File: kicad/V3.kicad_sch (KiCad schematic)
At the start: 6 parts, among them SW1 Slide_Switch_SPDT_P3mm_10x5x1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

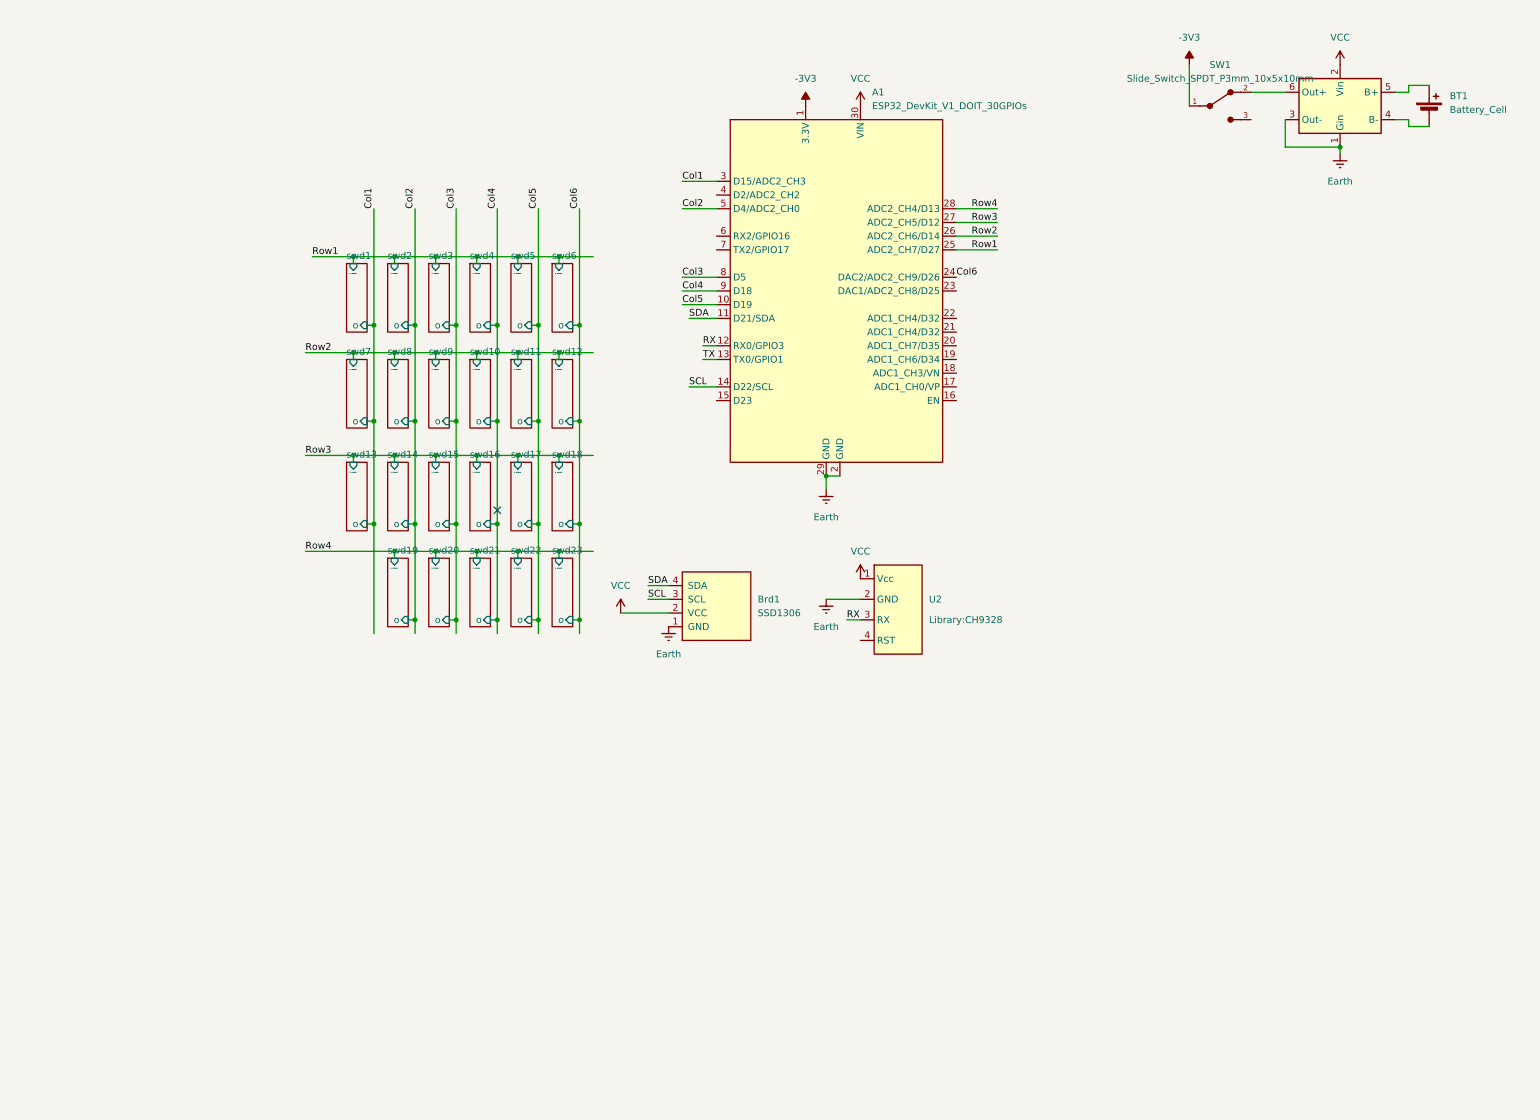
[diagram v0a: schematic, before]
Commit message: power
shouldnt be charging and discharging now i think
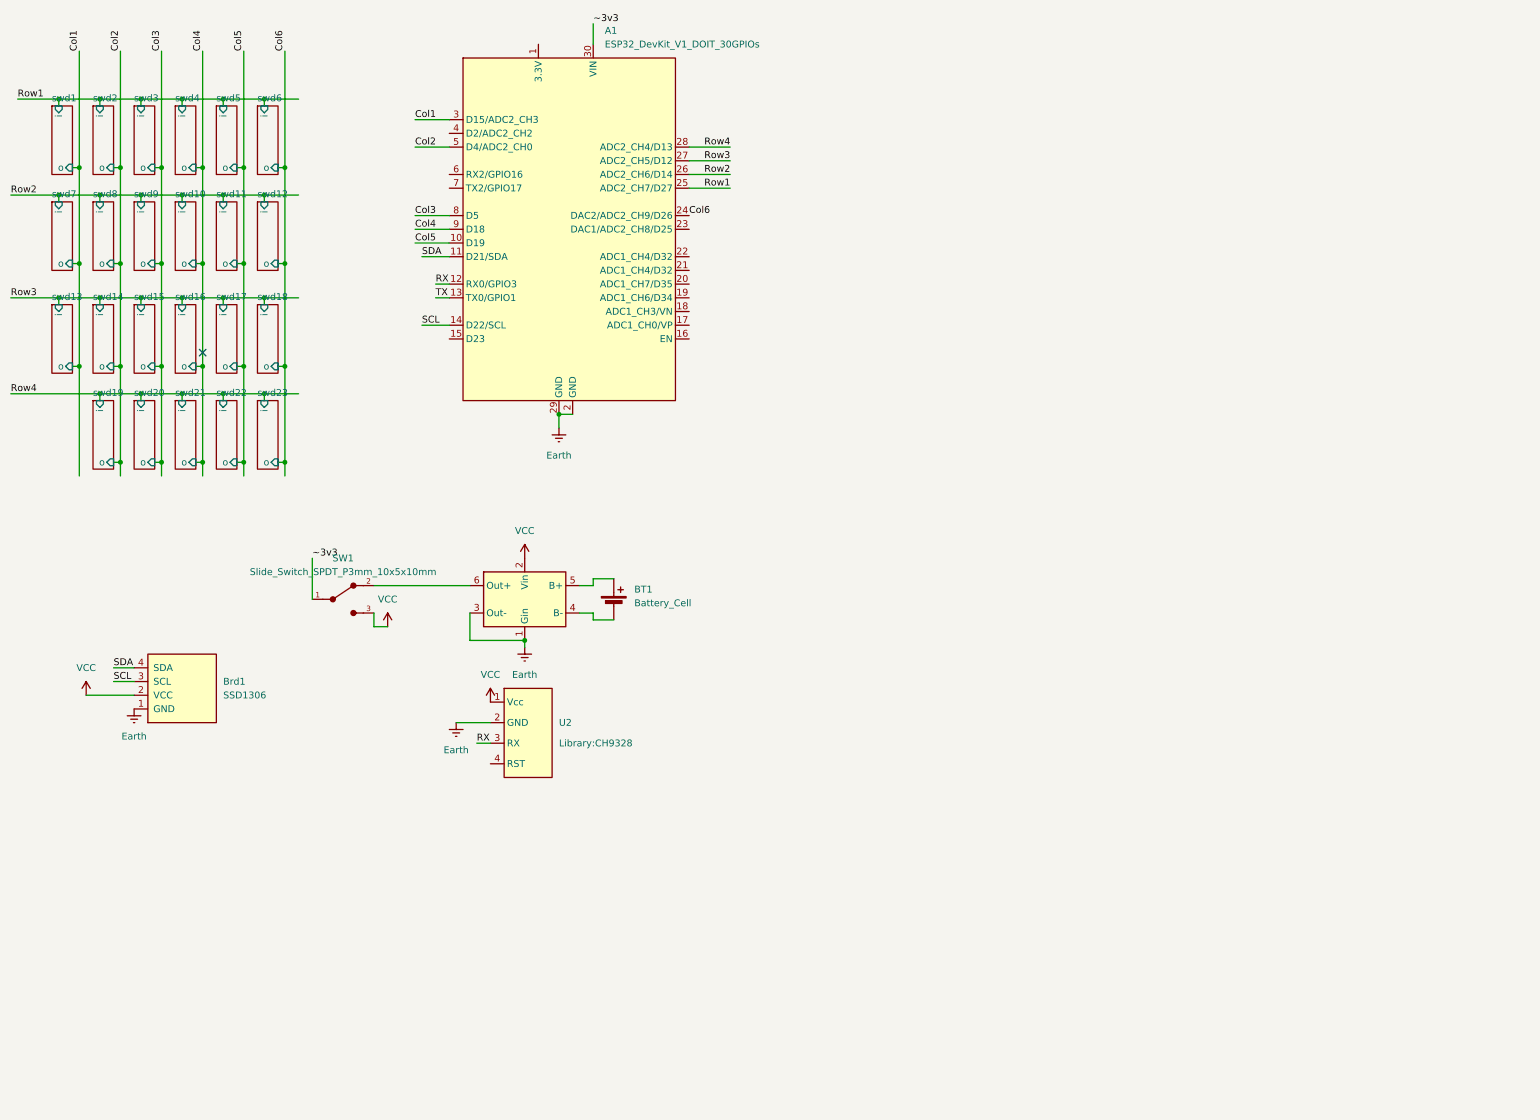
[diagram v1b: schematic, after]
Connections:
- net VCC: now also SW1.3; no longer A1.30 (VIN)
- net -3V3: no longer names the net of A1.1 (3.3V)
- net -3V3: no longer SW1.1
- new net ~3v3: A1.30 (VIN), SW1.1
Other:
- moved on the sheet: A1, BT1, Brd1, SW1, U2

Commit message: lots of changes
usb module support and more fixed wirign
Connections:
- net ~3v3: now also Brd1.2 (VCC)
- net USB_rst: now reaches A1.20 (ADC1_CH7/D35)
- net USB_rst: now also U2.4 (RST)
- net VCC renamed +5V
- net +5V: no longer Brd1.2 (VCC)
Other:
- moved on the sheet: SW1

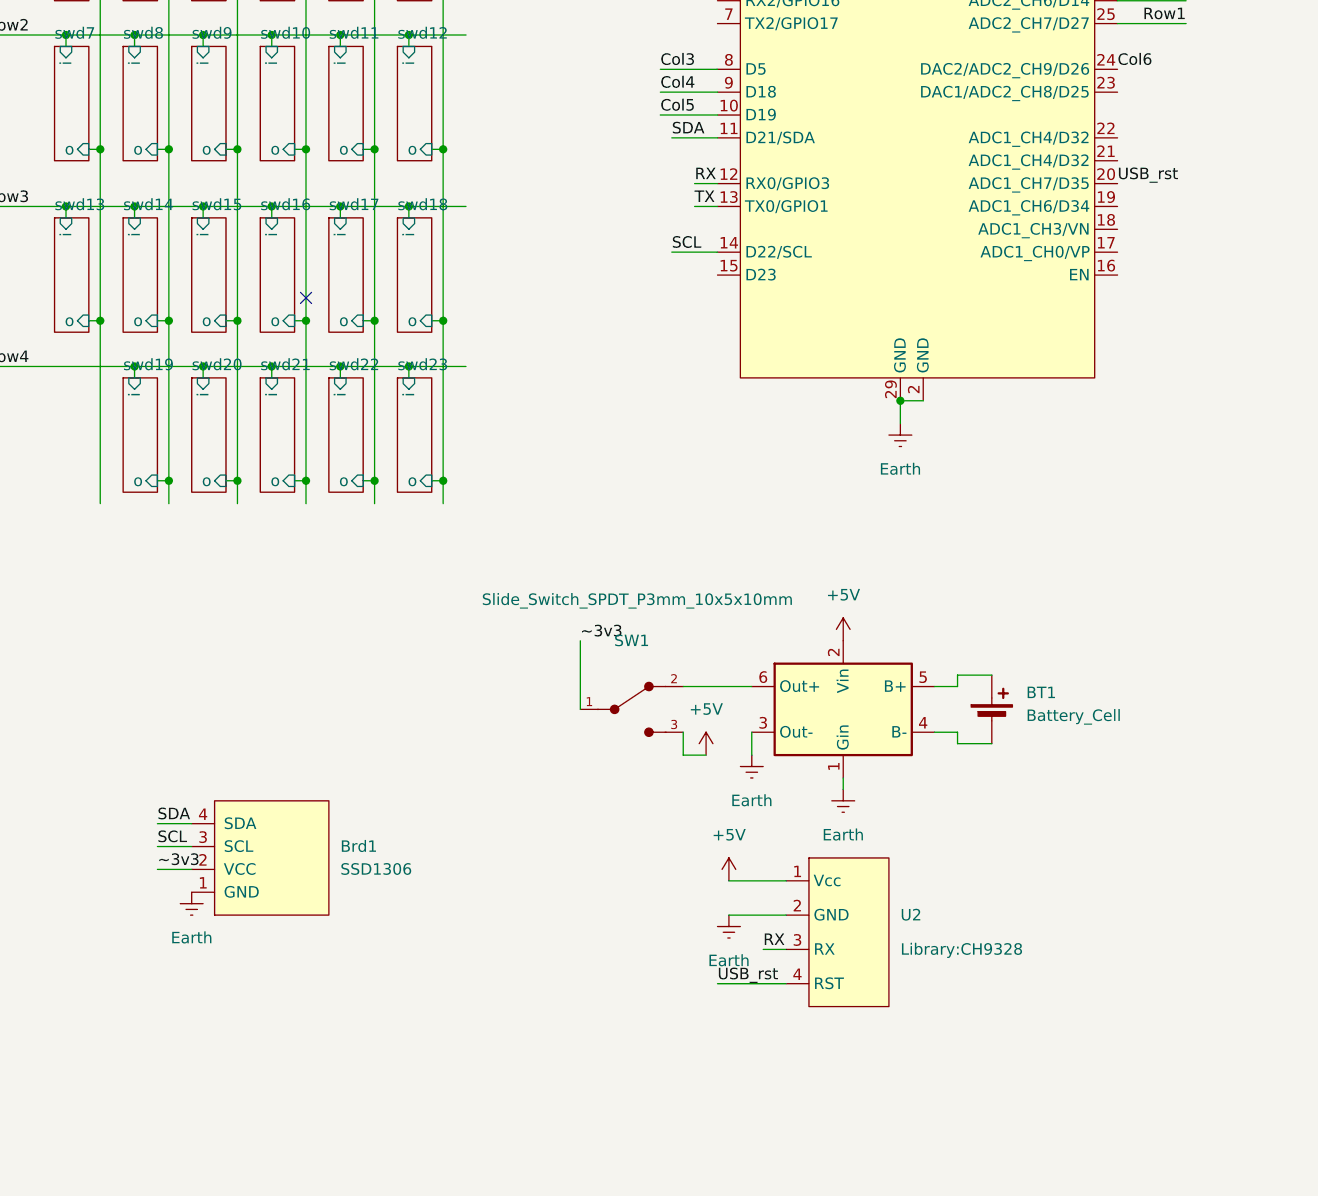
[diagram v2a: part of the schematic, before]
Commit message: schmatic changes
voltage divider now used for batter ypercentage calculation.
power-OR used as voltage supply
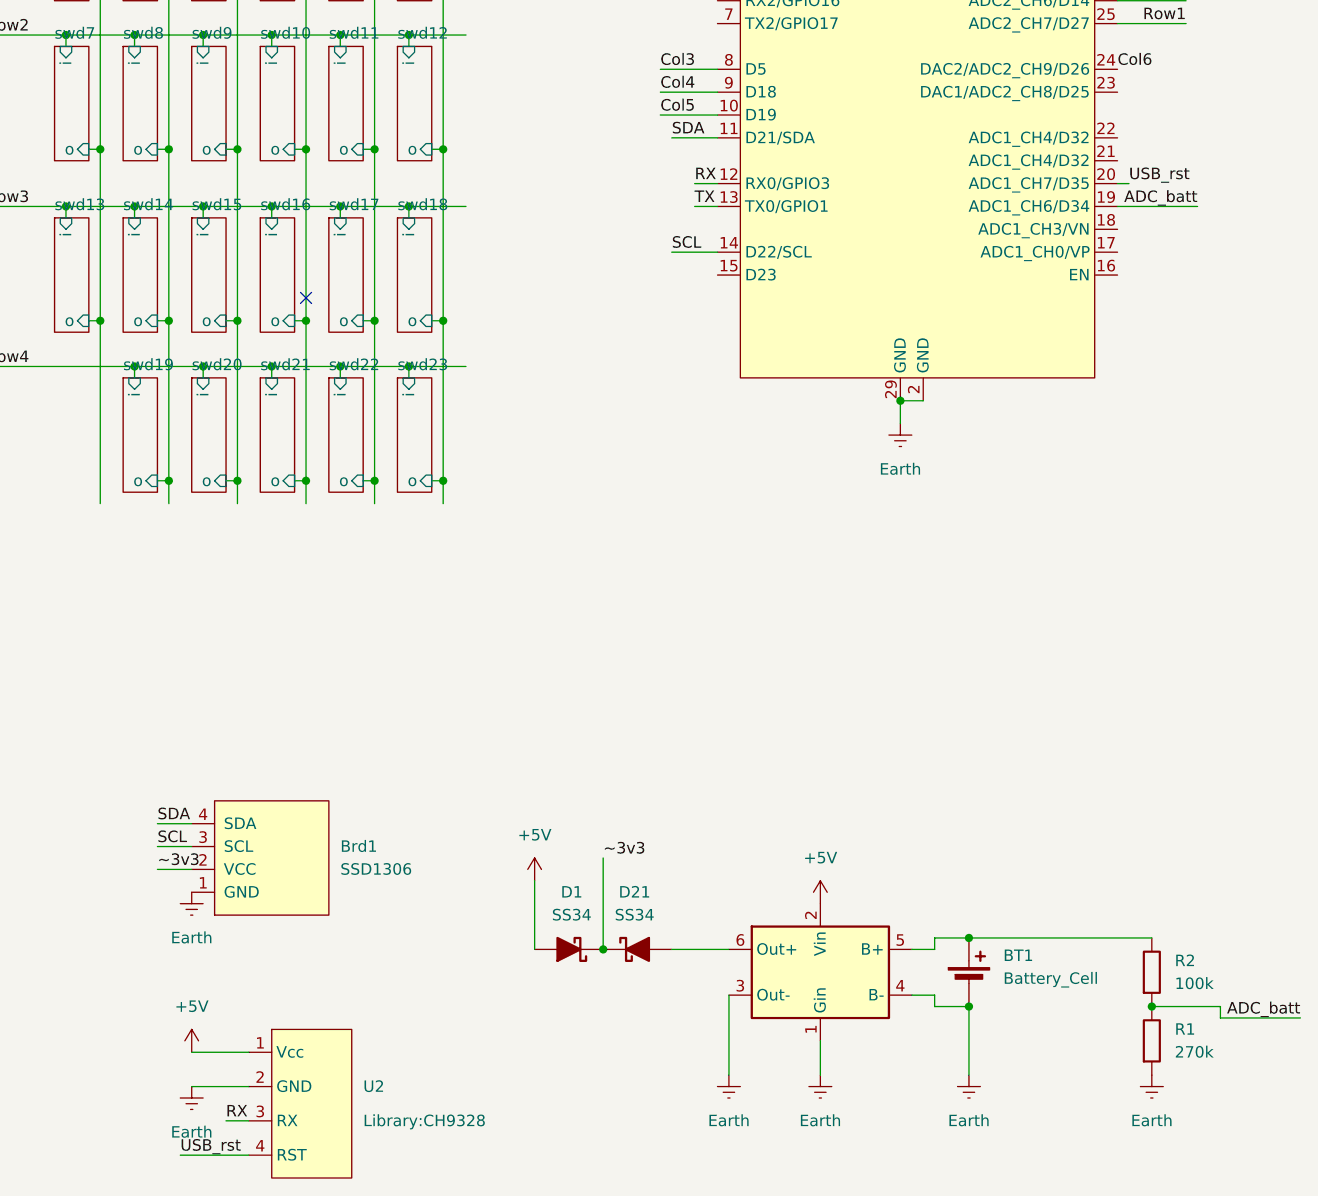
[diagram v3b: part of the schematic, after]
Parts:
- removed SW1: Slide_Switch_SPDT_P3mm_10x5x10mm, PCM_SL_Devices:Slide_Switch_SPDT_P3mm_10x5x10mm, symbol PCM_SL_Devices:Slide_Switch_SPDT_P3mm_10x5x10mm
- added D1, D21: SS34, PCM_Diode_SMD_AKL:D_SMC, symbol PCM_Diode_Schottky_AKL:SS34
- added R1: 270k, Resistor_THT:R_Axial_DIN0207_L6.3mm_D2.5mm_P10.16mm_Horizontal, symbol PCM_SL_Resistors:270k
- added R2: 100k, Resistor_THT:R_Axial_DIN0207_L6.3mm_D2.5mm_P10.16mm_Horizontal, symbol PCM_SL_Resistors:100k
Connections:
- net +5V: now also D1.2 (A)
- net Earth: now also BT1.2 (-), U1.4 (B-), R1.1
- net ~3v3: now also D1.1 (K), D21.1 (K)
- net ADC_batt: now reaches A1.19 (ADC1_CH6/D34)
- net ADC_batt: now also R1.2, R2.1
- net at BT1.1 (+), U1.5 (B+): now also R2.2
- net at U1.6 (Out+): now also D21.2 (A)
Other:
- moved on the sheet: BT1, U2

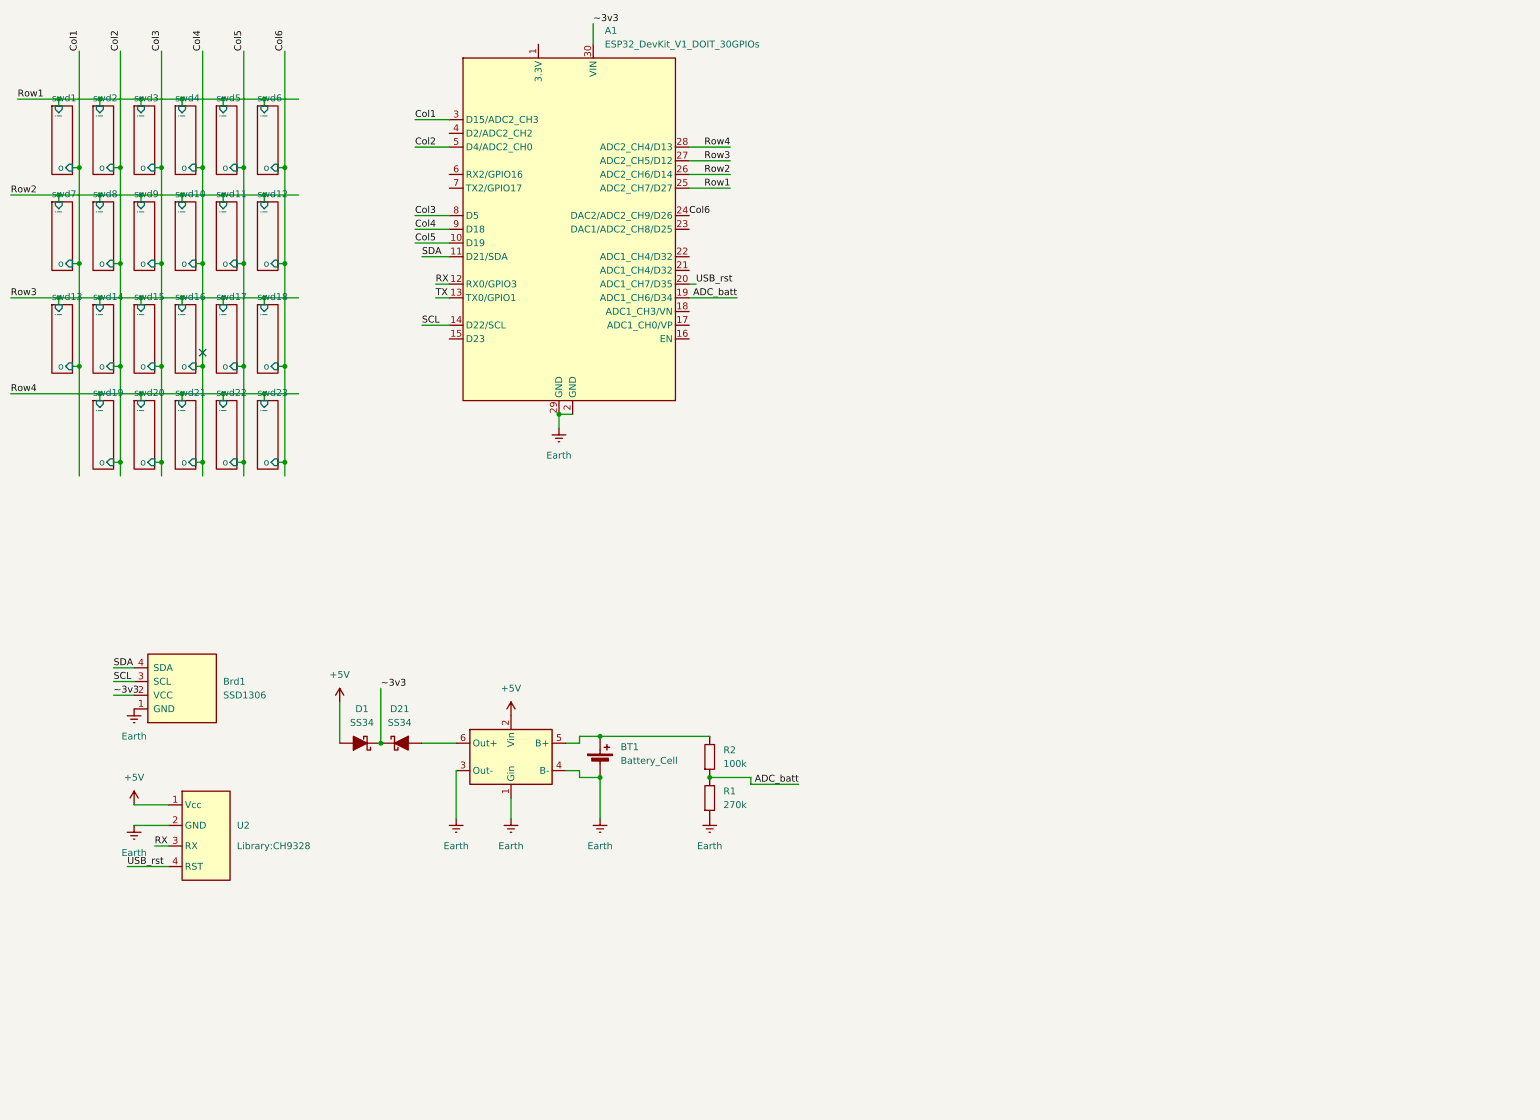
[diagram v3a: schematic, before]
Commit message: chip change
changed the module to use the ch9329(chip) instead of the ch9328 (board)
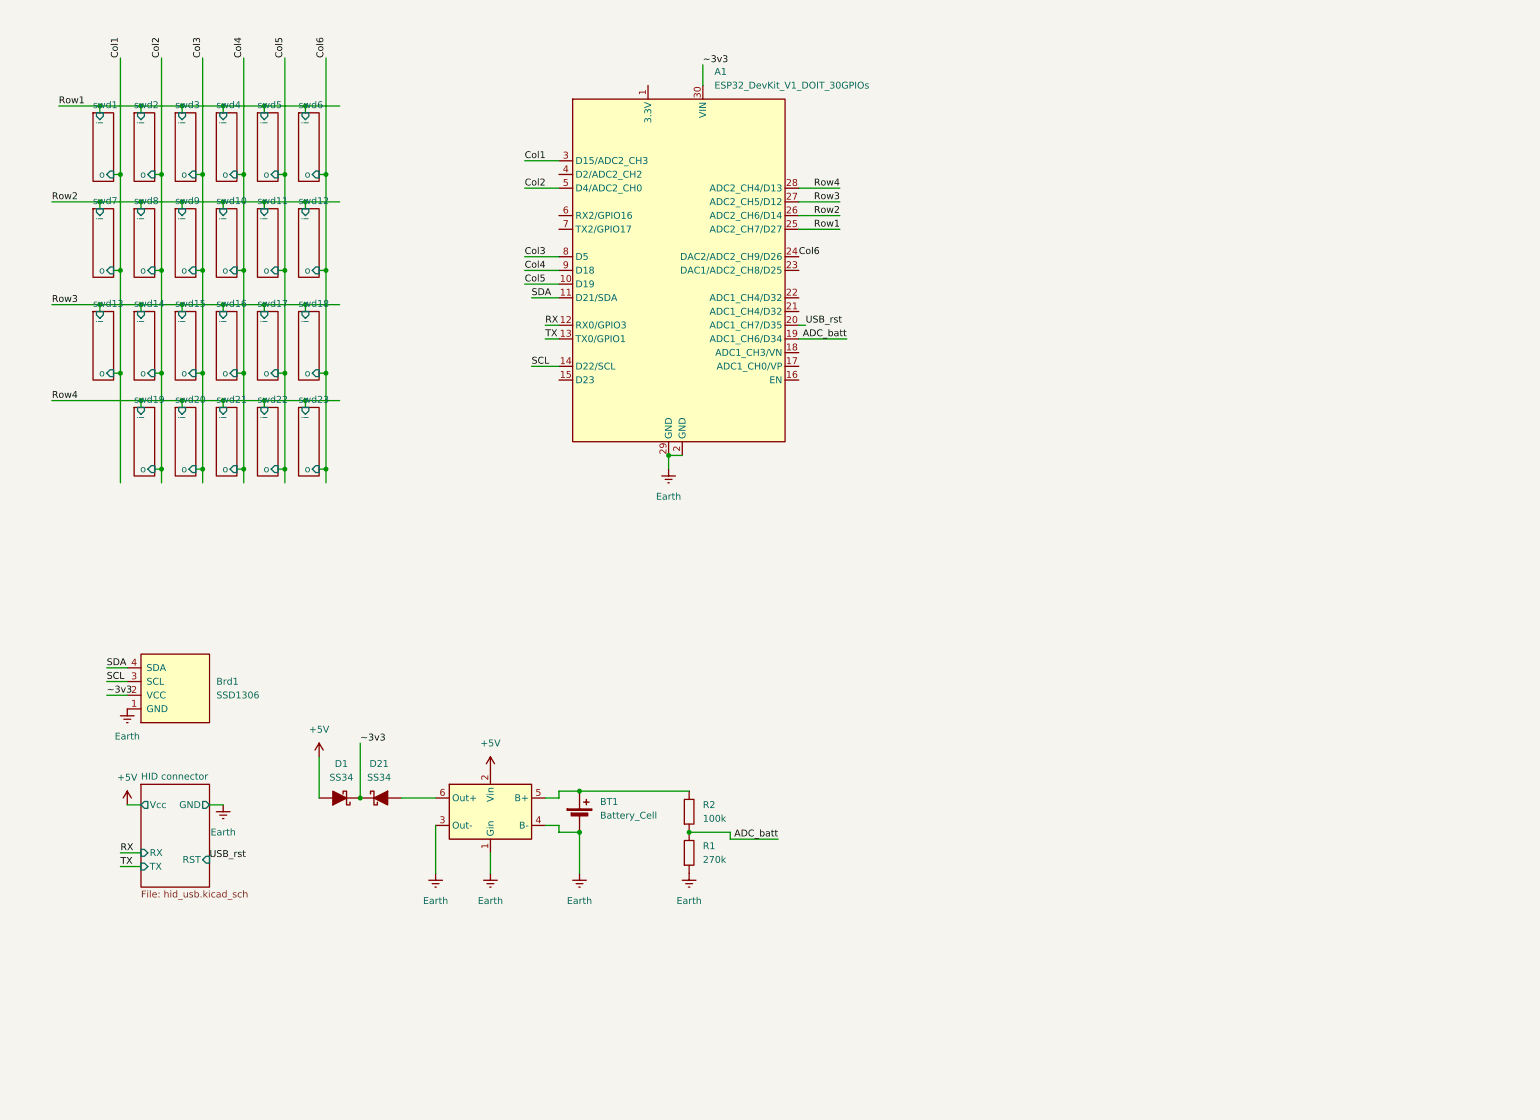
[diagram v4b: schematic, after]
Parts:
- removed U2: ~, Library:CH9328, symbol Library:CH9328
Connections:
- no-connect marks 1 -> 0
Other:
- added sheet HID connector (hid_usb.kicad_sch)
- moved on the sheet: A1, BT1, Brd1, D1, D21, R1, R2

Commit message: idk
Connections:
- net B+: now reaches BT1.1 (+), R2.2, U1.5 (B+)
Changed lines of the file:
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@@
-	)
-	(junction
-		(at 118.11 158.75)
-		(diameter 0)
-		(color 0 0 0 0)
 	)
 	(junction
@@
 		(pts
 			(xy 111.76 160.02) (xy 114.3 160.02)
-		)
-		(stroke
-			(width 0)
-			(type default)
-		)
-	)
-	(wire
-		(pts
-			(xy 118.11 158.75) (xy 138.43 158.75)
 		)
 		(stroke
@@
 		(effects
 			(font
+				(size 1.27 1.27)
+			)
+			(justify left bottom)
+		)
+	)
+	(label "B+"
+		(at 118.11 158.75 0)
+		(effects
+			(font
+				(size 1.27 1.27)
+			)
+			(justify left bottom)
+		)
+	)
+	(label "B+"
+		(at 138.43 158.75 0)
+		(effects
+			(font
